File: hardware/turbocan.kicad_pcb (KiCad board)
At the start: 2 copper layers, 43 x 43 mm, 88 parts, among them J1 USB_C_Receptacle_USB2.0, J10 CAN_PORT, J11 FAN0, J12 FAN1, J13 HEAT, J14 PROBE, J2 STEPPER, J5 DEBUG, J7 ENDSTOPX, J8 ENDSTOPY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

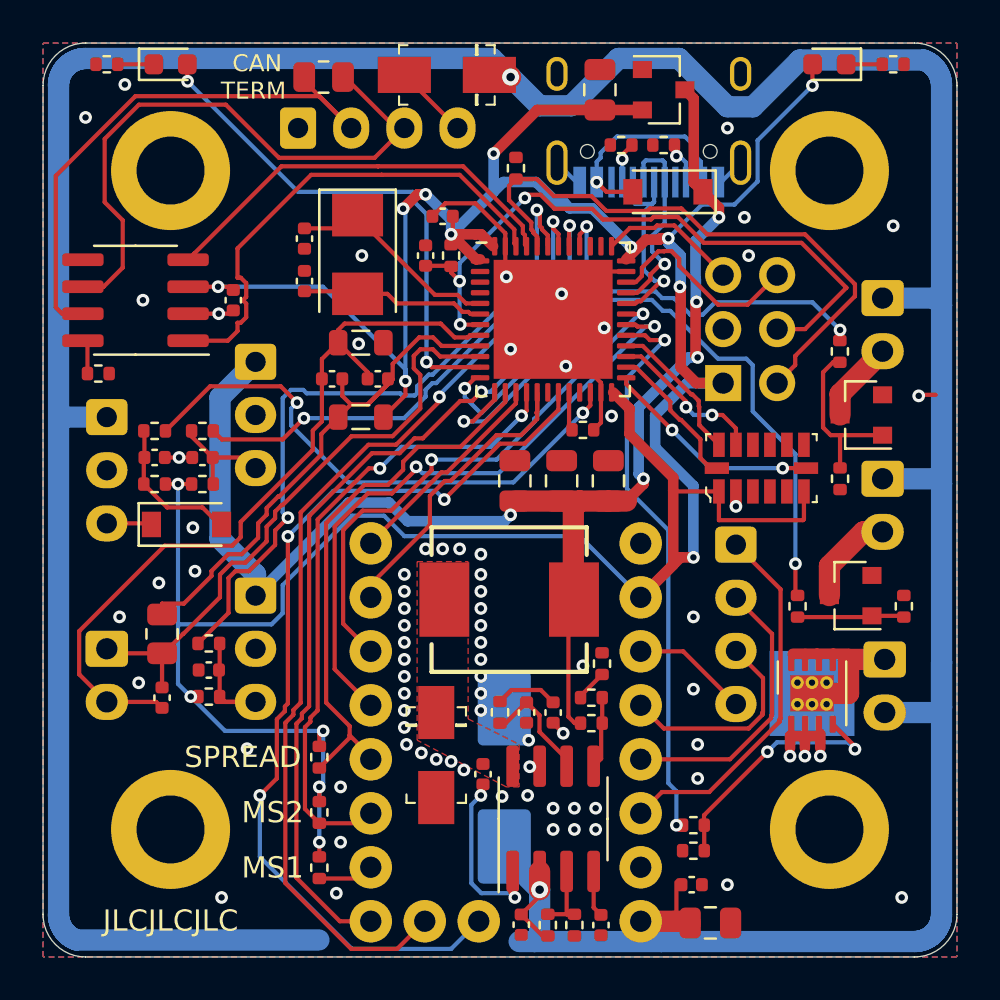
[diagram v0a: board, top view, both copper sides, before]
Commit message: update to kicad 6.0, assign a few parts with LCSC attributes
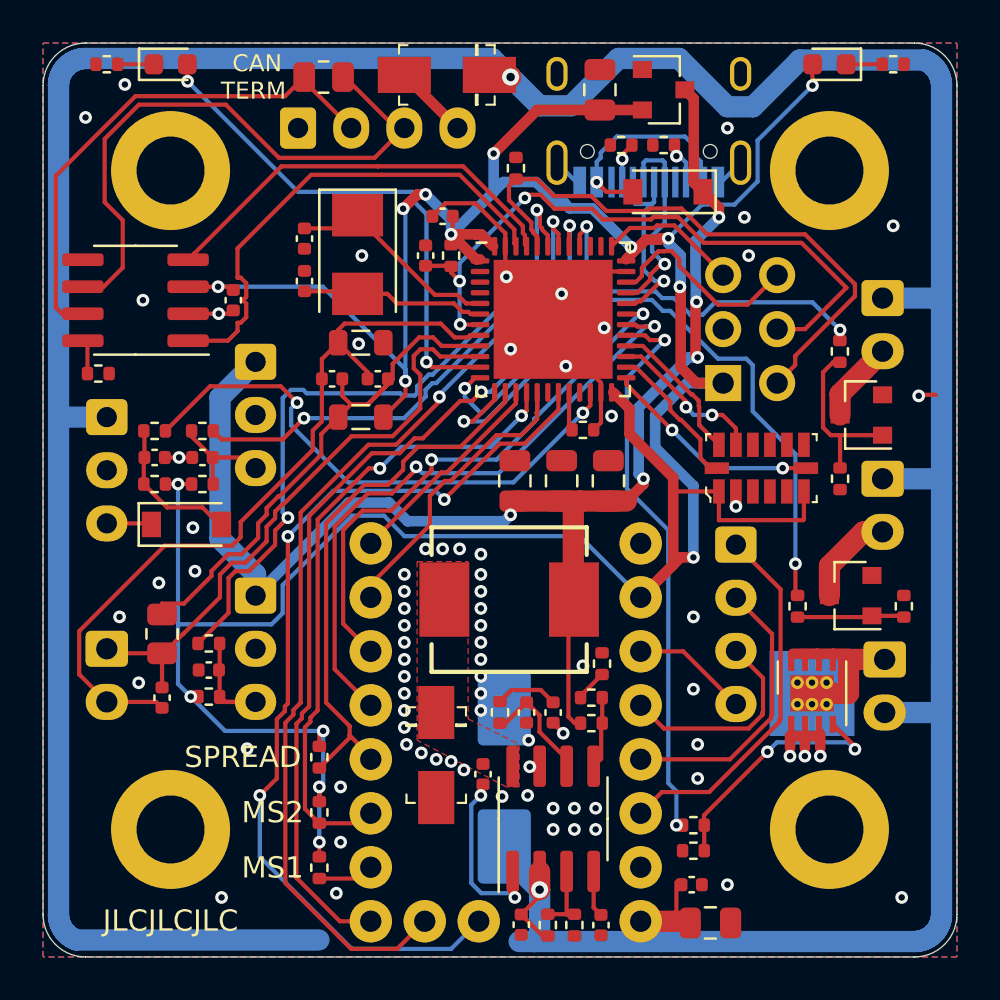
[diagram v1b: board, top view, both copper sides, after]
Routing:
- net CANH: track 27.0 -> 24.6 mm
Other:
- net class 0.5mm removed
- net class 1mm removed
- net class Default removed

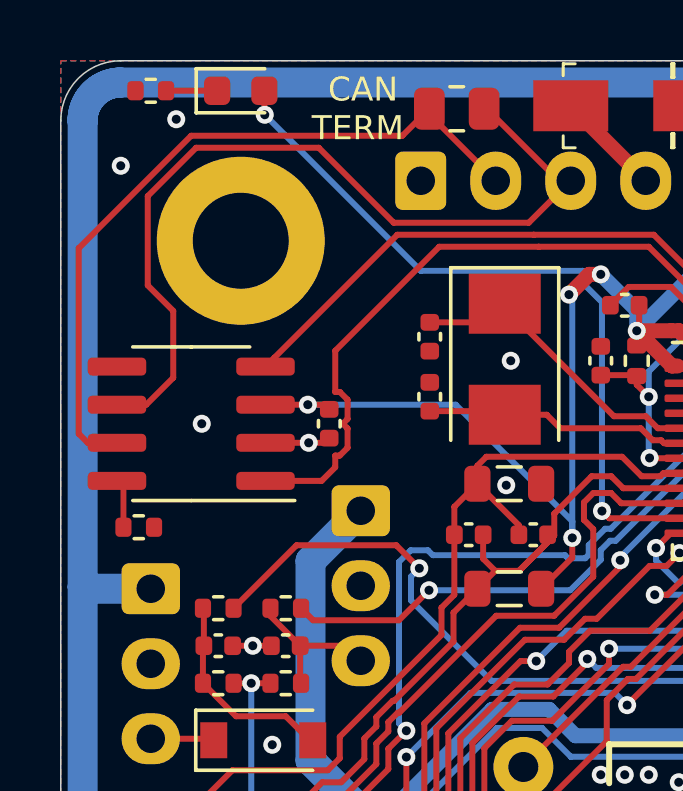
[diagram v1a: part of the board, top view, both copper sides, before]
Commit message: add solder jumper to probe supply (to select between 5v and 24v for PINDA)
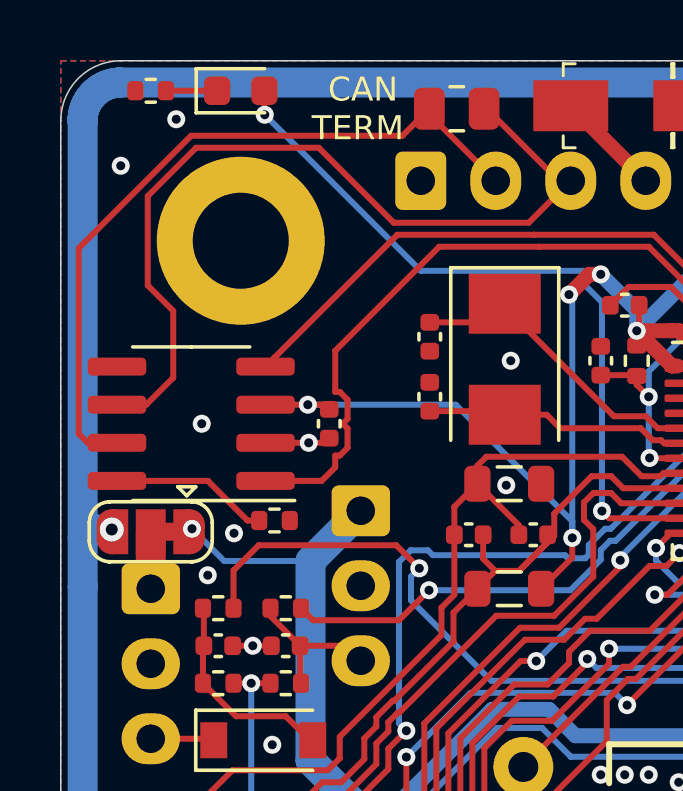
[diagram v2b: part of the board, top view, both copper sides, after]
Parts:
- added JP1: VPROBE, Jumper:SolderJumper-3_P1.3mm_Bridged12_RoundedPad1.0x1.5mm, F.Cu at (17.0, 29.7)
- moved R3 4.53 mm to (21.1, 29.3)
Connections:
- J1 pad A8: (no net) -> unconnected-(J1-PadA8)
- J1 pad B8: (no net) -> unconnected-(J1-PadB8)
- J14 pad 1: +24V -> Net-(J14-Pad1)
- U3 pad 5: (no net) -> unconnected-(U3-Pad5)
- U8 pad 18: (no net) -> unconnected-(U8-Pad18)
- U8 pad 2: (no net) -> unconnected-(U8-Pad2)
- U8 pad 21: (no net) -> unconnected-(U8-Pad21)
- U8 pad 3: (no net) -> unconnected-(U8-Pad3)
- U8 pad 38: (no net) -> unconnected-(U8-Pad38)
- U8 pad 39: (no net) -> unconnected-(U8-Pad39)
- U8 pad 4: (no net) -> unconnected-(U8-Pad4)
- U9 pad 10: (no net) -> unconnected-(U9-Pad10)
- U9 pad 11: (no net) -> unconnected-(U9-Pad11)
- U9 pad 3: (no net) -> unconnected-(U9-Pad3)
- U9 pad 8: (no net) -> unconnected-(U9-Pad8)
- U9 pad 9: (no net) -> unconnected-(U9-Pad9)
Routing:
- net +5V: track 66.1 -> 70.6 mm, vias 5 -> 6
- net Net-(R3-Pad1): track 1.63 -> 5.29 mm
- net Net-(J14-Pad1): track 0.00 -> 1.90 mm
- net +24V: track 187.6 -> 186.2 mm, vias 2 -> 3
- net PROBEZ: track 25.9 -> 26.6 mm
- net GND: vias 78 -> 80
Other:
- board text added: "24V/5V"
- board text removed: "24V"
